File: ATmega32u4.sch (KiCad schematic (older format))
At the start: 34 parts, among them J1 USB_B_Mini, J2 AVR-ISP-6, J3 Conn_01x04, SW70 SW_Push, U1 ATmega32U4-MU, Y1 16MHz

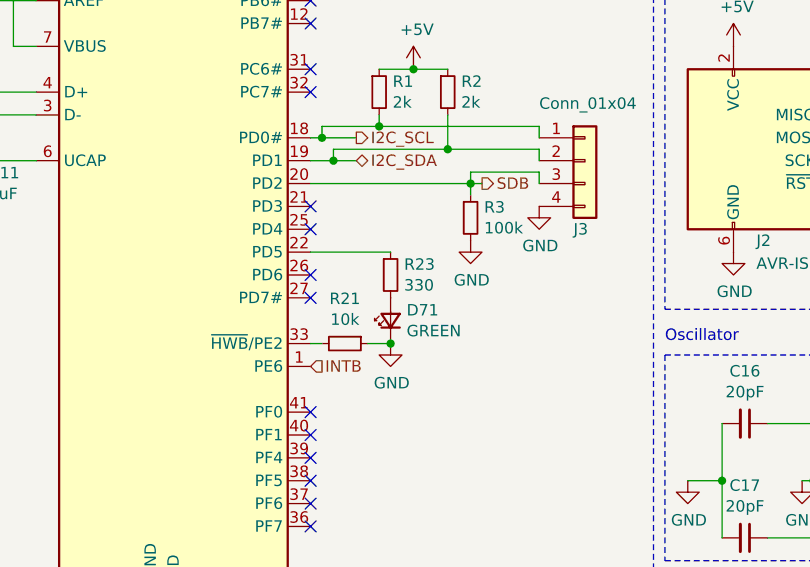
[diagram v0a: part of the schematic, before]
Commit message: Remove diodes, update interrupt connections
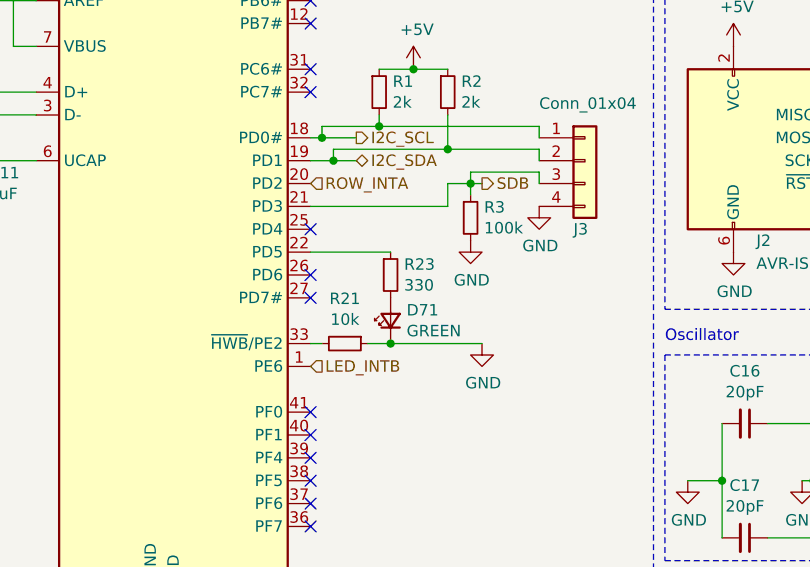
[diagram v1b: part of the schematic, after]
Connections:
- net SDB: now also U1.21 (PD3); no longer U1.20 (PD2)
- net INTB renamed LED_INTB
- new net ROW_INTA: U1.20 (PD2)
- no-connect marks 17 -> 16
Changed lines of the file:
@@
 L power:GND #PWR?
 U 1 1 61F97E33
-P 2750 3600
+P 3150 3600
 AR Path="/61F97E33" Ref="#PWR?"  Part="1"
 AR Path="/61F7F1B9/61F97E33" Ref="#PWR0117"  Part="1"
-F 0 "#PWR0117" H 2750 3350 50  0001 C CNN
-F 1 "GND" H 2755 3427 50  0000 C CNN
-F 2 "" H 2750 3600 50  0001 C CNN
-F 3 "" H 2750 3600 50  0001 C CNN
-	1    2750 3600
+F 0 "#PWR0117" H 3150 3350 50  0001 C CNN
+F 1 "GND" H 3155 3427 50  0000 C CNN
+F 2 "" H 3150 3600 50  0001 C CNN
+F 3 "" H 3150 3600 50  0001 C CNN
+	1    3150 3600
 	1    0    0    -1
 $EndComp
@@
 Wire Wire Line
 	3400 2850 3400 2900
-Wire Wire Line
-	2400 2900 3100 2900
 Connection ~ 3100 2900
 Wire Wire Line
@@
 	3100 2950 3100 2900
 Text HLabel 2400 3700 2    50   Input ~ 0
-INTB
-NoConn ~ 2400 3000
+LED_INTB
+Wire Wire Line
+	2400 3000 3000 3000
+Wire Wire Line
+	3000 3000 3000 2900
+Wire Wire Line
+	3000 2900 3100 2900
+Text HLabel 2400 2900 2    50   Input ~ 0
+ROW_INTA
+Wire Wire Line
+	3150 3600 2750 3600
 $EndSCHEMATC

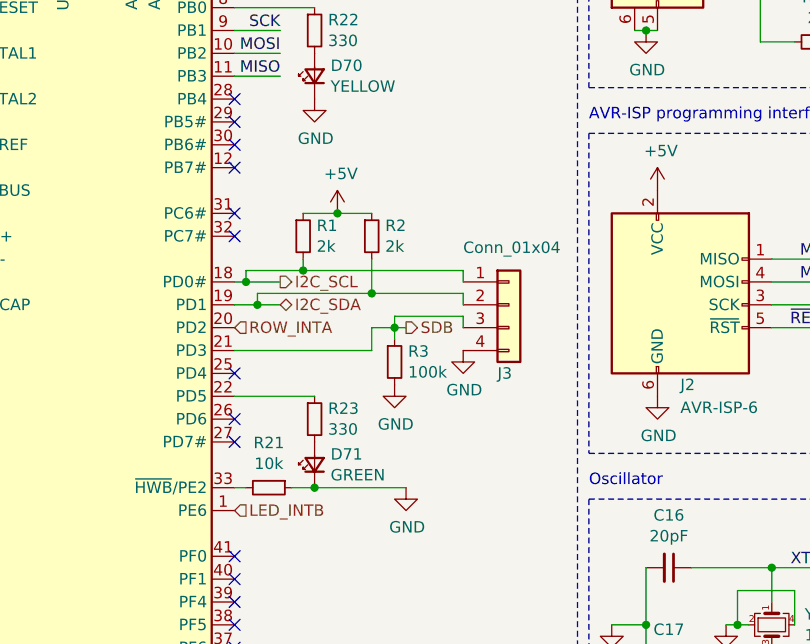
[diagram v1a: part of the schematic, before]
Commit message: Add ROW INTB, new debug header
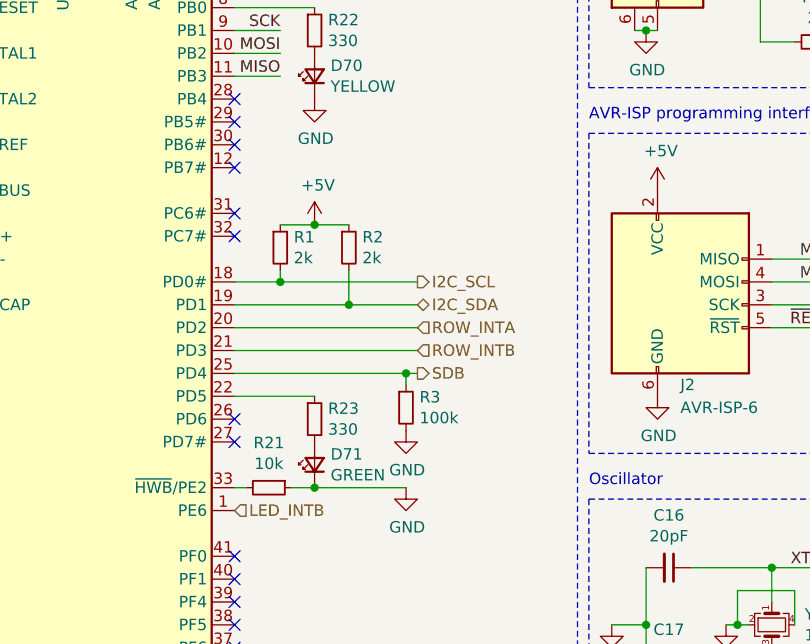
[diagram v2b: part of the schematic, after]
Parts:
- removed J3: Conn_01x04, Connector_PinHeader_2.54mm:PinHeader_1x04_P2.54mm_Vertical, symbol Connector_Generic:Conn_01x04
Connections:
- net SDB: now also U1.25 (PD4); no longer U1.21 (PD3)
- new net ROW_INTB: U1.21 (PD3)
- no-connect marks 16 -> 15
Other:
- moved on the sheet: R1, R2, R3
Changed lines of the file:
@@
 NoConn ~ 2400 2400
 NoConn ~ 2400 2500
-NoConn ~ 2400 3100
 NoConn ~ 2400 3300
 NoConn ~ 2400 3400
@@
 	2050 1200 1950 1200
 Connection ~ 1950 1200
-Text HLabel 2600 2700 2    50   Output ~ 0
+Text HLabel 3200 2700 2    50   Output ~ 0
 I2C_SCL
-Text HLabel 2600 2800 2    50   BiDi ~ 0
+Text HLabel 3200 2800 2    50   BiDi ~ 0
 I2C_SDA
-Wire Wire Line
-	2400 2800 2500 2800
-Text HLabel 3150 2900 2    50   Output ~ 0
+Text HLabel 3200 3100 2    50   Output ~ 0
 SDB
-Wire Wire Line
-	2500 2800 2500 2750
-Wire Wire Line
-	2500 2750 3000 2750
-Connection ~ 2500 2800
-Wire Wire Line
-	2500 2800 2600 2800
-Wire Wire Line
-	2400 2700 2450 2700
-Wire Wire Line
-	2450 2700 2450 2650
-Connection ~ 2450 2700
-Wire Wire Line
-	2450 2700 2600 2700
-$Comp
-L Connector_Generic:Conn_01x04 J3
-U 1 1 618E5A1D
-P 3600 2800
-F 0 "J3" H 3550 2500 50  0000 L CNN
-F 1 "Conn_01x04" H 3400 3050 50  0000 L CNN
-F 2 "Connector_PinHeader_2.54mm:PinHeader_1x04_P2.54mm_Vertical" H 3600 2800 50  0001 C CNN
-F 3 "~" H 3600 2800 50  0001 C CNN
-	1    3600 2800
-	1    0    0    -1
-$EndComp
-$Comp
-L power:GND #PWR0105
-U 1 1 618E6506
-P 3400 3000
-F 0 "#PWR0105" H 3400 2750 50  0001 C CNN
-F 1 "GND" H 3405 2827 50  0000 C CNN
-F 2 "" H 3400 3000 50  0001 C CNN
-F 3 "" H 3400 3000 50  0001 C CNN
-	1    3400 3000
-	1    0    0    -1
-$EndComp
 $Comp
 L Device:R_Small R1
 U 1 1 6192799E
-P 2700 2500
-F 0 "R1" H 2759 2546 50  0000 L CNN
-F 1 "2k" H 2759 2455 50  0000 L CNN
-F 2 "Resistor_SMD:R_0805_2012Metric_Pad1.20x1.40mm_HandSolder" H 2700 2500 50  0001 C CNN
-F 3 "~" H 2700 2500 50  0001 C CNN
-F 4 "0805" H 2700 2500 50  0001 C CNN "JLC"
-F 5 "C17604" H 2700 2500 50  0001 C CNN "LCSC"
-	1    2700 2500
+P 2600 2550
+F 0 "R1" H 2659 2596 50  0000 L CNN
+F 1 "2k" H 2659 2505 50  0000 L CNN
+F 2 "Resistor_SMD:R_0805_2012Metric_Pad1.20x1.40mm_HandSolder" H 2600 2550 50  0001 C CNN
+F 3 "~" H 2600 2550 50  0001 C CNN
+F 4 "0805" H 2600 2550 50  0001 C CNN "JLC"
+F 5 "C17604" H 2600 2550 50  0001 C CNN "LCSC"
+	1    2600 2550
 	1    0    0    -1
 $EndComp
@@
 L Device:R_Small R2
 U 1 1 619283FA
-P 3000 2500
-F 0 "R2" H 3059 2546 50  0000 L CNN
-F 1 "2k" H 3059 2455 50  0000 L CNN
-F 2 "Resistor_SMD:R_0805_2012Metric_Pad1.20x1.40mm_HandSolder" H 3000 2500 50  0001 C CNN
-F 3 "~" H 3000 2500 50  0001 C CNN
-F 4 "0805" H 3000 2500 50  0001 C CNN "JLC"
-F 5 "C17604" H 3000 2500 50  0001 C CNN "LCSC"
-	1    3000 2500
-	1    0    0    -1
-$EndComp
-Wire Wire Line
-	2450 2650 2700 2650
-Wire Wire Line
-	2700 2650 2700 2600
-Connection ~ 2700 2650
+P 2900 2550
+F 0 "R2" H 2959 2596 50  0000 L CNN
+F 1 "2k" H 2959 2505 50  0000 L CNN
+F 2 "Resistor_SMD:R_0805_2012Metric_Pad1.20x1.40mm_HandSolder" H 2900 2550 50  0001 C CNN
+F 3 "~" H 2900 2550 50  0001 C CNN
+F 4 "0805" H 2900 2550 50  0001 C CNN "JLC"
+F 5 "C17604" H 2900 2550 50  0001 C CNN "LCSC"
+	1    2900 2550
+	1    0    0    -1
+$EndComp
+Wire Wire Line
+	2600 2700 2600 2650
 $Comp
 L power:+5V #PWR06
 U 1 1 6193D3D5
-P 2850 2400
-F 0 "#PWR06" H 2850 2250 50  0001 C CNN
-F 1 "+5V" H 2865 2573 50  0000 C CNN
-F 2 "" H 2850 2400 50  0001 C CNN
-F 3 "" H 2850 2400 50  0001 C CNN
-	1    2850 2400
-	1    0    0    -1
-$EndComp
-Wire Wire Line
-	3000 2750 3000 2600
-Connection ~ 3000 2750
-Wire Wire Line
-	2700 2400 2850 2400
-Connection ~ 2850 2400
-Wire Wire Line
-	2850 2400 3000 2400
+P 2750 2450
+F 0 "#PWR06" H 2750 2300 50  0001 C CNN
+F 1 "+5V" H 2765 2623 50  0000 C CNN
+F 2 "" H 2750 2450 50  0001 C CNN
+F 3 "" H 2750 2450 50  0001 C CNN
+	1    2750 2450
+	1    0    0    -1
+$EndComp
+Wire Wire Line
+	2900 2800 2900 2650
+Wire Wire Line
+	2600 2450 2750 2450
+Connection ~ 2750 2450
+Wire Wire Line
+	2750 2450 2900 2450
+Text HLabel 2400 3700 2    50   Input ~ 0
+LED_INTB
+Text HLabel 3200 2900 2    50   Input ~ 0
+ROW_INTA
+Wire Wire Line
+	3150 3600 2750 3600
+Wire Wire Line
+	2400 2700 2600 2700
+Wire Wire Line
+	2600 2700 3200 2700
+Connection ~ 2600 2700
+Wire Wire Line
+	2400 2800 2900 2800
+Connection ~ 2900 2800
+Wire Wire Line
+	2900 2800 3200 2800
+$Comp
+L Device:R_Small R?
+U 1 1 61951368
+P 3150 3250
+AR Path="/61951368" Ref="R?"  Part="1"
+AR Path="/61F7F1B9/61951368" Ref="R3"  Part="1"
+F 0 "R3" H 3209 3296 50  0000 L CNN
+F 1 "100k" H 3209 3205 50  0000 L CNN
+F 2 "Resistor_SMD:R_0402_1005Metric" H 3150 3250 50  0001 C CNN
+F 3 "~" H 3150 3250 50  0001 C CNN
+F 4 "0402" H 3150 3250 50  0001 C CNN "JLC"
+F 5 "C25741" H 3150 3250 50  0001 C CNN "LCSC"
+	1    3150 3250
+	1    0    0    -1
+$EndComp
 $Comp
 L power:GND #PWR?
 U 1 1 6195136F
-P 3100 3150
+P 3150 3350
 AR Path="/6195136F" Ref="#PWR?"  Part="1"
 AR Path="/61F7F1B9/6195136F" Ref="#PWR012"  Part="1"
-F 0 "#PWR012" H 3100 2900 50  0001 C CNN
-F 1 "GND" H 3105 2977 50  0000 C CNN
-F 2 "" H 3100 3150 50  0001 C CNN
-F 3 "" H 3100 3150 50  0001 C CNN
-	1    3100 3150
-	1    0    0    -1
-$EndComp
-Wire Wire Line
-	3400 2850 3400 2900
-Connection ~ 3100 2900
-Wire Wire Line
-	3100 2900 3150 2900
-Wire Wire Line
-	3400 2850 3100 2850
-Wire Wire Line
-	3100 2850 3100 2900
-Wire Wire Line
-	3400 2750 3400 2800
-Wire Wire Line
-	3000 2750 3400 2750
-Wire Wire Line
-	3400 2650 3400 2700
-Wire Wire Line
-	2700 2650 3400 2650
-$Comp
-L Device:R_Small R?
-U 1 1 61951368
-P 3100 3050
-AR Path="/61951368" Ref="R?"  Part="1"
-AR Path="/61F7F1B9/61951368" Ref="R3"  Part="1"
-F 0 "R3" H 3159 3096 50  0000 L CNN
-F 1 "100k" H 3159 3005 50  0000 L CNN
-F 2 "Resistor_SMD:R_0402_1005Metric" H 3100 3050 50  0001 C CNN
-F 3 "~" H 3100 3050 50  0001 C CNN
-F 4 "0402" H 3100 3050 50  0001 C CNN "JLC"
-F 5 "C25741" H 3100 3050 50  0001 C CNN "LCSC"
-	1    3100 3050
-	1    0    0    -1
-$EndComp
-Wire Wire Line
-	3100 2950 3100 2900
-Text HLabel 2400 3700 2    50   Input ~ 0
-LED_INTB
-Wire Wire Line
-	2400 3000 3000 3000
-Wire Wire Line
-	3000 3000 3000 2900
-Wire Wire Line
-	3000 2900 3100 2900
-Text HLabel 2400 2900 2    50   Input ~ 0
-ROW_INTA
-Wire Wire Line
-	3150 3600 2750 3600
+F 0 "#PWR012" H 3150 3100 50  0001 C CNN
+F 1 "GND" H 3155 3177 50  0000 C CNN
+F 2 "" H 3150 3350 50  0001 C CNN
+F 3 "" H 3150 3350 50  0001 C CNN
+	1    3150 3350
+	1    0    0    -1
+$EndComp
+Wire Wire Line
+	3150 3150 3150 3100
+Wire Wire Line
+	3200 2900 2400 2900
+Wire Wire Line
+	2400 3100 3150 3100
+Wire Wire Line
+	3200 3100 3150 3100
+Connection ~ 3150 3100
+Wire Wire Line
+	2400 3000 3200 3000
+Text HLabel 3200 3000 2    50   Input ~ 0
+ROW_INTB
 $EndSCHEMATC

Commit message: Use perfect 0402 pad dimensions
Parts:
- C10, C11, C12, C13, C14, C15, C16, C17, C18, C19, C20, C9: footprint Capacitor_SMD:C_0402_1005Metric -> Collins-FMS-3000:Perfect_0402
- R21, R22, R23, R24, R25, R26, R27, R28, R3: footprint Resistor_SMD:R_0402_1005Metric -> Collins-FMS-3000:Perfect_0402
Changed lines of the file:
@@
 F 0 "C10" H 892 1046 50  0000 L CNN
 F 1 "10uF" H 892 955 50  0000 L CNN
-F 2 "Capacitor_SMD:C_0402_1005Metric" H 800 1000 50  0001 C CNN
+F 2 "Collins-FMS-3000:Perfect_0402" H 800 1000 50  0001 C CNN
 F 3 "~" H 800 1000 50  0001 C CNN
 F 4 "0402" H 800 1000 50  0001 C CNN "JLC"
@@
 F 0 "C9" H 792 2246 50  0000 L CNN
 F 1 "1uF" H 792 2155 50  0000 L CNN
-F 2 "Capacitor_SMD:C_0402_1005Metric" H 700 2200 50  0001 C CNN
+F 2 "Collins-FMS-3000:Perfect_0402" H 700 2200 50  0001 C CNN
 F 3 "~" H 700 2200 50  0001 C CNN
 F 4 "0402" H 700 2200 50  0001 C CNN "JLC"
@@
 F 0 "C11" H 992 2946 50  0000 L CNN
 F 1 "1uF" H 992 2855 50  0000 L CNN
-F 2 "Capacitor_SMD:C_0402_1005Metric" H 900 2900 50  0001 C CNN
+F 2 "Collins-FMS-3000:Perfect_0402" H 900 2900 50  0001 C CNN
 F 3 "~" H 900 2900 50  0001 C CNN
 F 4 "0402" H 900 2900 50  0001 C CNN "JLC"
@@
 F 0 "R22" H 2809 1646 50  0000 L CNN
 F 1 "330" H 2809 1555 50  0000 L CNN
-F 2 "Resistor_SMD:R_0402_1005Metric" H 2750 1600 50  0001 C CNN
+F 2 "Collins-FMS-3000:Perfect_0402" H 2750 1600 50  0001 C CNN
 F 3 "~" H 2750 1600 50  0001 C CNN
 F 4 "0402" H 2750 1600 50  0001 C CNN "JLC"
@@
 F 0 "R23" H 2809 3346 50  0000 L CNN
 F 1 "330" H 2809 3255 50  0000 L CNN
-F 2 "Resistor_SMD:R_0402_1005Metric" H 2750 3300 50  0001 C CNN
+F 2 "Collins-FMS-3000:Perfect_0402" H 2750 3300 50  0001 C CNN
 F 3 "~" H 2750 3300 50  0001 C CNN
 F 4 "0402" H 2750 3300 50  0001 C CNN "JLC"
@@
 F 0 "R21" V 2354 3600 50  0000 C CNN
 F 1 "10k" V 2445 3600 50  0000 C CNN
-F 2 "Resistor_SMD:R_0402_1005Metric" H 2550 3600 50  0001 C CNN
+F 2 "Collins-FMS-3000:Perfect_0402" H 2550 3600 50  0001 C CNN
 F 3 "~" H 2550 3600 50  0001 C CNN
 F 4 "0402" H 2550 3600 50  0001 C CNN "JLC"
@@
 F 0 "C12" H 2392 1046 50  0000 L CNN
 F 1 "100nf" H 2392 955 50  0000 L CNN
-F 2 "Capacitor_SMD:C_0402_1005Metric" H 2300 1000 50  0001 C CNN
+F 2 "Collins-FMS-3000:Perfect_0402" H 2300 1000 50  0001 C CNN
 F 3 "~" H 2300 1000 50  0001 C CNN
 F 4 "0402" H 2300 1000 50  0001 C CNN "JLC"
@@
 F 0 "C13" H 2792 1046 50  0000 L CNN
 F 1 "100nf" H 2792 955 50  0000 L CNN
-F 2 "Capacitor_SMD:C_0402_1005Metric" H 2700 1000 50  0001 C CNN
+F 2 "Collins-FMS-3000:Perfect_0402" H 2700 1000 50  0001 C CNN
 F 3 "~" H 2700 1000 50  0001 C CNN
 F 4 "0402" H 2700 1000 50  0001 C CNN "JLC"
@@
 F 0 "C14" H 3192 1046 50  0000 L CNN
 F 1 "100nf" H 3192 955 50  0000 L CNN
-F 2 "Capacitor_SMD:C_0402_1005Metric" H 3100 1000 50  0001 C CNN
+F 2 "Collins-FMS-3000:Perfect_0402" H 3100 1000 50  0001 C CNN
 F 3 "~" H 3100 1000 50  0001 C CNN
 F 4 "0402" H 3100 1000 50  0001 C CNN "JLC"
@@
 F 0 "C15" H 3592 1046 50  0000 L CNN
 F 1 "100nf" H 3592 955 50  0000 L CNN
-F 2 "Capacitor_SMD:C_0402_1005Metric" H 3500 1000 50  0001 C CNN
+F 2 "Collins-FMS-3000:Perfect_0402" H 3500 1000 50  0001 C CNN
 F 3 "~" H 3500 1000 50  0001 C CNN
 F 4 "0402" H 3500 1000 50  0001 C CNN "JLC"
@@
 F 0 "R24" V 4754 1350 50  0000 C CNN
 F 1 "22" V 4845 1350 50  0000 C CNN
-F 2 "Resistor_SMD:R_0402_1005Metric" H 4950 1350 50  0001 C CNN
+F 2 "Collins-FMS-3000:Perfect_0402" H 4950 1350 50  0001 C CNN
 F 3 "~" H 4950 1350 50  0001 C CNN
 F 4 "0402" H 4950 1350 50  0001 C CNN "JLC"
@@
 F 0 "R25" V 4754 1650 50  0000 C CNN
 F 1 "22" V 4845 1650 50  0000 C CNN
-F 2 "Resistor_SMD:R_0402_1005Metric" H 4950 1650 50  0001 C CNN
+F 2 "Collins-FMS-3000:Perfect_0402" H 4950 1650 50  0001 C CNN
 F 3 "~" H 4950 1650 50  0001 C CNN
 F 4 "0402" H 4950 1650 50  0001 C CNN "JLC"
@@
 F 0 "C18" H 5542 1146 50  0000 L CNN
 F 1 "10uF" H 5542 1055 50  0000 L CNN
-F 2 "Capacitor_SMD:C_0402_1005Metric" H 5450 1100 50  0001 C CNN
+F 2 "Collins-FMS-3000:Perfect_0402" H 5450 1100 50  0001 C CNN
 F 3 "~" H 5450 1100 50  0001 C CNN
 F 4 "0402" H 5450 1100 50  0001 C CNN "JLC"
@@
 F 0 "R28" H 5959 1146 50  0000 L CNN
 F 1 "1K" H 5959 1055 50  0000 L CNN
-F 2 "Resistor_SMD:R_0402_1005Metric" H 5900 1100 50  0001 C CNN
+F 2 "Collins-FMS-3000:Perfect_0402" H 5900 1100 50  0001 C CNN
 F 3 "~" H 5900 1100 50  0001 C CNN
 F 4 "0402" H 5900 1100 50  0001 C CNN "JLC"
@@
 F 0 "C16" V 4071 3950 50  0000 C CNN
 F 1 "20pF" V 4162 3950 50  0000 C CNN
-F 2 "Capacitor_SMD:C_0402_1005Metric" H 4300 3950 50  0001 C CNN
+F 2 "Collins-FMS-3000:Perfect_0402" H 4300 3950 50  0001 C CNN
 F 3 "~" H 4300 3950 50  0001 C CNN
 F 4 "0402" H 4300 3950 50  0001 C CNN "JLC"
@@
 F 0 "C17" V 4071 4450 50  0000 C CNN
 F 1 "20pF" V 4162 4450 50  0000 C CNN
-F 2 "Capacitor_SMD:C_0402_1005Metric" H 4300 4450 50  0001 C CNN
+F 2 "Collins-FMS-3000:Perfect_0402" H 4300 4450 50  0001 C CNN
 F 3 "~" H 4300 4450 50  0001 C CNN
 F 4 "0402" H 4300 4450 50  0001 C CNN "JLC"
@@
 F 0 "C20" H 6292 2446 50  0000 L CNN
 F 1 "100nf" H 6292 2355 50  0000 L CNN
-F 2 "Capacitor_SMD:C_0402_1005Metric" H 6200 2400 50  0001 C CNN
+F 2 "Collins-FMS-3000:Perfect_0402" H 6200 2400 50  0001 C CNN
 F 3 "~" H 6200 2400 50  0001 C CNN
 F 4 "0402" H 6200 2400 50  0001 C CNN "JLC"
@@
 F 0 "C19" H 5892 2446 50  0000 L CNN
 F 1 "100nf" H 5892 2355 50  0000 L CNN
-F 2 "Capacitor_SMD:C_0402_1005Metric" H 5800 2400 50  0001 C CNN
+F 2 "Collins-FMS-3000:Perfect_0402" H 5800 2400 50  0001 C CNN
 F 3 "~" H 5800 2400 50  0001 C CNN
 F 4 "0402" H 5800 2400 50  0001 C CNN "JLC"
@@
 F 0 "R27" H 5459 2446 50  0000 L CNN
 F 1 "10k" H 5459 2355 50  0000 L CNN
-F 2 "Resistor_SMD:R_0402_1005Metric" H 5400 2400 50  0001 C CNN
+F 2 "Collins-FMS-3000:Perfect_0402" H 5400 2400 50  0001 C CNN
 F 3 "~" H 5400 2400 50  0001 C CNN
 F 4 "0402" H 5400 2400 50  0001 C CNN "JLC"
@@
 F 0 "R26" V 5446 3200 50  0000 C CNN
 F 1 "330" V 5355 3200 50  0000 C CNN
-F 2 "Resistor_SMD:R_0402_1005Metric" H 5250 3200 50  0001 C CNN
+F 2 "Collins-FMS-3000:Perfect_0402" H 5250 3200 50  0001 C CNN
 F 3 "~" H 5250 3200 50  0001 C CNN
 F 4 "0402" H 5250 3200 50  0001 C CNN "JLC"
@@
 F 0 "R3" H 3209 3296 50  0000 L CNN
 F 1 "100k" H 3209 3205 50  0000 L CNN
-F 2 "Resistor_SMD:R_0402_1005Metric" H 3150 3250 50  0001 C CNN
+F 2 "Collins-FMS-3000:Perfect_0402" H 3150 3250 50  0001 C CNN
 F 3 "~" H 3150 3250 50  0001 C CNN
 F 4 "0402" H 3150 3250 50  0001 C CNN "JLC"
